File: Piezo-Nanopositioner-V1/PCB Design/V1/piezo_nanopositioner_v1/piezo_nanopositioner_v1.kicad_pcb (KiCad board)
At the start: 2 copper layers, 7 parts, among them J2 RF2-04A-T-00-50-G, U1 TDA2050, U2 DAC0800LCM, U3 TL431AIDBZR, U4 TL431AIDBZR

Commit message: finalized schematic, added hierarchical sheets for X,Y,Z circuit. Added all part fingerprints.
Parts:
- added C11: 47u, Capacitor_SMD:CAP_EEFC_E_PAN, F.Cu at (199.4, 137.6)
- added C13: 100uF 50V, Capacitor_THT:CAP_YX_8X11P5_RUB, F.Cu at (247.7, 123.4)
- added C14: 10n, Capacitor_SMD:C_0805_2012Metric, F.Cu at (186.8, 101.9)
- added C15: 100n, Capacitor_SMD:C_0805_2012Metric, F.Cu at (186.8, 104.9)
- added C16: 100n, Capacitor_SMD:C_0805_2012Metric, F.Cu at (186.8, 107.9)
- added C17: 470u, Capacitor_THT:CAP_ZSU_G12_PAN, F.Cu at (177.7, 106.5)
- added C18: 470u, Capacitor_THT:CAP_ZSU_G12_PAN, F.Cu at (177.7, 118.6)
- added C19: 68p, Capacitor_SMD:C_0805_2012Metric, F.Cu at (186.8, 110.9)
- added C20: 100n, Capacitor_SMD:C_0805_2012Metric, F.Cu at (186.8, 113.9)
- added C21: 100n, Capacitor_SMD:C_0805_2012Metric, F.Cu at (186.8, 116.9)
- added C22: 4.7n, Capacitor_SMD:C_0805_2012Metric, F.Cu at (186.8, 119.9)
- added C23: 47u, Capacitor_SMD:CAP_EEFC_E_PAN, F.Cu at (222.0, 89.0)
- added C24: 10n, Capacitor_SMD:C_0805_2012Metric, F.Cu at (209.4, 53.3)
- added C25: 100n, Capacitor_SMD:C_0805_2012Metric, F.Cu at (209.4, 56.3)
- added C26: 100n, Capacitor_SMD:C_0805_2012Metric, F.Cu at (209.4, 59.3)
- added C27: 470u, Capacitor_THT:CAP_ZSU_G12_PAN, F.Cu at (200.2, 57.8)
- added C28: 470u, Capacitor_THT:CAP_ZSU_G12_PAN, F.Cu at (200.2, 70.0)
- added C29: 68p, Capacitor_SMD:C_0805_2012Metric, F.Cu at (209.4, 62.3)
- added C30: 100n, Capacitor_SMD:C_0805_2012Metric, F.Cu at (209.4, 65.3)
- added C31: 100n, Capacitor_SMD:C_0805_2012Metric, F.Cu at (209.4, 68.3)
- added C32: 4.7n, Capacitor_SMD:C_0805_2012Metric, F.Cu at (209.4, 71.3)
- added C33: 47u, Capacitor_SMD:CAP_EEFC_E_PAN, F.Cu at (145.9, 90.5)
- added C34: 10n, Capacitor_SMD:C_0805_2012Metric, F.Cu at (133.2, 54.8)
- added C35: 100n, Capacitor_SMD:C_0805_2012Metric, F.Cu at (133.2, 57.8)
- added C36: 100n, Capacitor_SMD:C_0805_2012Metric, F.Cu at (133.2, 60.8)
- added C37: 470u, Capacitor_THT:CAP_ZSU_G12_PAN, F.Cu at (124.1, 59.0)
- added C38: 470u, Capacitor_THT:CAP_ZSU_G12_PAN, F.Cu at (110.5, 59.0)
- added C39: 68p, Capacitor_SMD:C_0805_2012Metric, F.Cu at (133.2, 63.8)
- added C40: 100n, Capacitor_SMD:C_0805_2012Metric, F.Cu at (133.2, 66.8)
- added C41: 100n, Capacitor_SMD:C_0805_2012Metric, F.Cu at (133.2, 69.8)
- added C42: 4.7n, Capacitor_SMD:C_0805_2012Metric, F.Cu at (133.2, 72.8)
- added D1: D, Diode_THT:DO-41_DIO, F.Cu at (246.1, 112.0)
- added D2: D, Diode_THT:DO-41_DIO, F.Cu at (246.1, 116.3)
- added J1: Conn_01x03_Pin, Connector_PinHeader_2.54mm:PinHeader_1x03_P2.54mm_Vertical, F.Cu at (256.8, 120.7)
- added J4: Conn_01x10_Pin, Connector_PinHeader_2.54mm:PinHeader_1x10_P2.54mm_Vertical, F.Cu at (167.8, 102.7)
- added J5: RF2-04A-T-00-50-G, RF:CONN_RF2-04A-T-00-50-G_ADM, F.Cu at (188.8, 137.3)
- added J6: Conn_01x10_Pin, Connector_PinHeader_2.54mm:PinHeader_1x10_P2.54mm_Vertical, F.Cu at (190.4, 54.1)
- added J7: RF2-04A-T-00-50-G, RF:CONN_RF2-04A-T-00-50-G_ADM, F.Cu at (211.4, 88.7)
- added J8: Conn_01x10_Pin, Connector_PinHeader_2.54mm:PinHeader_1x10_P2.54mm_Vertical, F.Cu at (117.4, 104.5)
- added J9: RF2-04A-T-00-50-G, RF:CONN_RF2-04A-T-00-50-G_ADM, F.Cu at (117.1, 48.6)
- added R14: 100R, Resistor_SMD:R_0805_2012Metric, F.Cu at (191.3, 101.8)
- added R15: 100R, Resistor_SMD:R_0805_2012Metric, F.Cu at (191.3, 104.8)
- added R16: 100R, Resistor_SMD:R_0805_2012Metric, F.Cu at (191.3, 107.8)
- added R17: 100R, Resistor_SMD:R_0805_2012Metric, F.Cu at (191.3, 110.7)
- added R18: 100R, Resistor_SMD:R_0805_2012Metric, F.Cu at (191.3, 113.7)
- added R19: 100R, Resistor_SMD:R_0805_2012Metric, F.Cu at (195.7, 101.8)
- added R20: 100R, Resistor_SMD:R_0805_2012Metric, F.Cu at (195.7, 104.8)
- added R21: 100R, Resistor_SMD:R_0805_2012Metric, F.Cu at (195.7, 107.8)
- added R22: 1k, Resistor_SMD:R_0805_2012Metric, F.Cu at (195.7, 110.7)
- added R23: 5k, Resistor_SMD:R_0805_2012Metric, F.Cu at (195.7, 113.7)
- added R24: 5k, Resistor_SMD:R_0805_2012Metric, F.Cu at (200.1, 101.8)
- added R25: 15k, Resistor_SMD:R_0805_2012Metric, F.Cu at (200.1, 104.8)
- added R26: 10R, Resistor_SMD:R_0805_2012Metric, F.Cu at (200.1, 107.8)
- added R27: 100R, Resistor_SMD:R_0805_2012Metric, F.Cu at (213.8, 53.2)
- added R28: 100R, Resistor_SMD:R_0805_2012Metric, F.Cu at (213.8, 56.2)
- added R29: 100R, Resistor_SMD:R_0805_2012Metric, F.Cu at (213.8, 59.1)
- added R30: 100R, Resistor_SMD:R_0805_2012Metric, F.Cu at (213.8, 62.1)
- added R31: 100R, Resistor_SMD:R_0805_2012Metric, F.Cu at (213.8, 65.0)
- added R32: 100R, Resistor_SMD:R_0805_2012Metric, F.Cu at (218.2, 53.2)
- added R33: 100R, Resistor_SMD:R_0805_2012Metric, F.Cu at (218.2, 56.2)
- added R34: 100R, Resistor_SMD:R_0805_2012Metric, F.Cu at (218.2, 59.1)
- added R35: 1k, Resistor_SMD:R_0805_2012Metric, F.Cu at (218.2, 62.1)
- added R36: 5k, Resistor_SMD:R_0805_2012Metric, F.Cu at (218.2, 65.0)
- added R37: 5k, Resistor_SMD:R_0805_2012Metric, F.Cu at (222.6, 53.2)
- added R38: 15k, Resistor_SMD:R_0805_2012Metric, F.Cu at (222.6, 56.2)
- added R39: 10R, Resistor_SMD:R_0805_2012Metric, F.Cu at (222.6, 59.1)
- added R40: 100R, Resistor_SMD:R_0805_2012Metric, F.Cu at (137.7, 54.7)
- added R41: 100R, Resistor_SMD:R_0805_2012Metric, F.Cu at (137.7, 57.7)
- added R42: 100R, Resistor_SMD:R_0805_2012Metric, F.Cu at (137.7, 60.6)
- added R43: 100R, Resistor_SMD:R_0805_2012Metric, F.Cu at (137.7, 63.6)
- added R44: 100R, Resistor_SMD:R_0805_2012Metric, F.Cu at (137.7, 66.5)
- added R45: 100R, Resistor_SMD:R_0805_2012Metric, F.Cu at (142.1, 54.7)
- added R46: 100R, Resistor_SMD:R_0805_2012Metric, F.Cu at (142.1, 57.7)
- added R47: 100R, Resistor_SMD:R_0805_2012Metric, F.Cu at (142.1, 60.6)
- added R48: 1k, Resistor_SMD:R_0805_2012Metric, F.Cu at (142.1, 63.6)
- added R49: 5k, Resistor_SMD:R_0805_2012Metric, F.Cu at (142.1, 66.5)
- added R50: 5k, Resistor_SMD:R_0805_2012Metric, F.Cu at (146.5, 54.7)
- added R51: 15k, Resistor_SMD:R_0805_2012Metric, F.Cu at (146.5, 57.7)
- added R52: 10R, Resistor_SMD:R_0805_2012Metric, F.Cu at (146.5, 60.6)
- added RV2: 10k, Potentiometer_THT:TRIM_COM-09806, F.Cu at (199.5, 127.0)
- added RV3: 10k, Potentiometer_THT:TRIM_COM-09806, F.Cu at (222.1, 78.4)
- added RV4: 10k, Potentiometer_THT:TRIM_COM-09806, F.Cu at (146.0, 79.9)
- added U10: TL431AIDBZR, TL431AIDBZR:DBZ0003A_N, F.Cu at (119.0, 90.5)
- added U11: DAC0800LCM, DAC0800LCM_SMT:M16A_TEX, F.Cu at (135.3, 80.2)
- added U12: TDA2050, Package_TO_SOT_THT:TO-220-5_P3.4x3.7mm_StaggerOdd_Lead3.8mm_Vertical, F.Cu at (118.9, 86.5)
- added U3: TL431AIDBZR, TL431AIDBZR:DBZ0003A_N, F.Cu at (172.6, 137.6)
- added U5: DAC0800LCM, DAC0800LCM_SMT:M16A_TEX, F.Cu at (188.9, 127.3)
- added U6: TDA2050, Package_TO_SOT_THT:TO-220-5_P3.4x3.7mm_StaggerOdd_Lead3.8mm_Vertical, F.Cu at (172.5, 133.7)
- added U7: TL431AIDBZR, TL431AIDBZR:DBZ0003A_N, F.Cu at (195.2, 89.0)
- added U8: DAC0800LCM, DAC0800LCM_SMT:M16A_TEX, F.Cu at (211.5, 78.7)
- added U9: TDA2050, Package_TO_SOT_THT:TO-220-5_P3.4x3.7mm_StaggerOdd_Lead3.8mm_Vertical, F.Cu at (195.1, 85.0)
- C12: value 50YXJ100MT78X11.5 -> 100uF 50V
- moved U4 83.9 mm to (56.5, 96.5)
- moved C12 83.9 mm to (43.0, 98.5)
- moved Heatsink 83.9 mm to (58.2, 74.5)
- moved J2 83.9 mm to (28.5, 98.0)
- moved U1 83.9 mm to (54.9, 86.2)
- moved U2 83.9 mm to (30.7, 71.1)
- moved U3 83.9 mm to (30.5, 81.0)
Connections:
- C12 pad 1: unconnected-(C12-Pad1) -> GND
- C12 pad 2: unconnected-(C12-Pad2) -> -15V

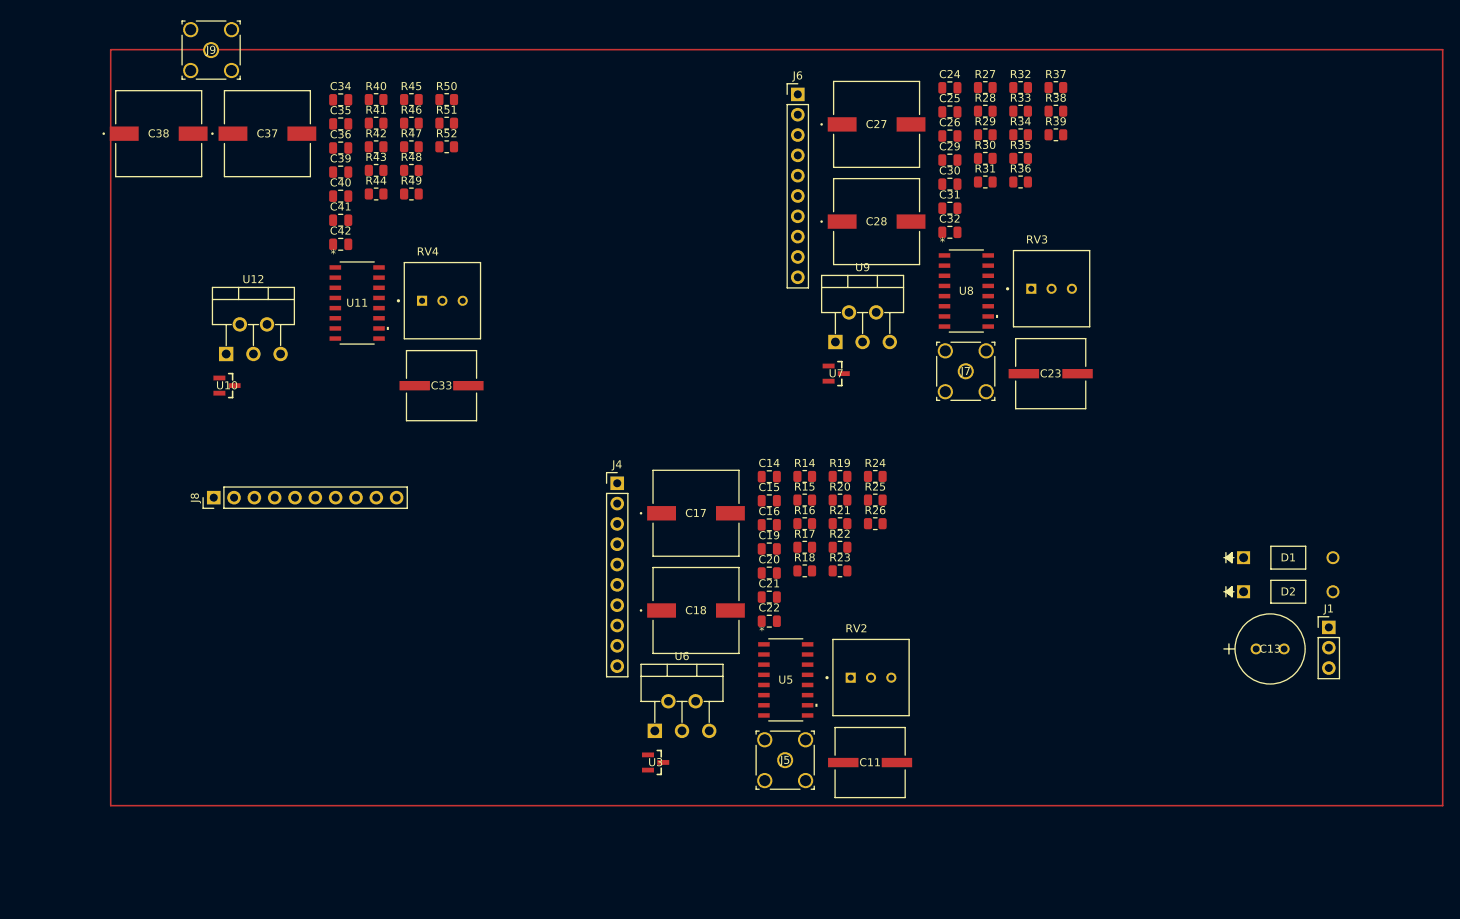
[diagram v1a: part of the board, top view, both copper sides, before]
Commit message: started PCB design, almost finished first DAC.
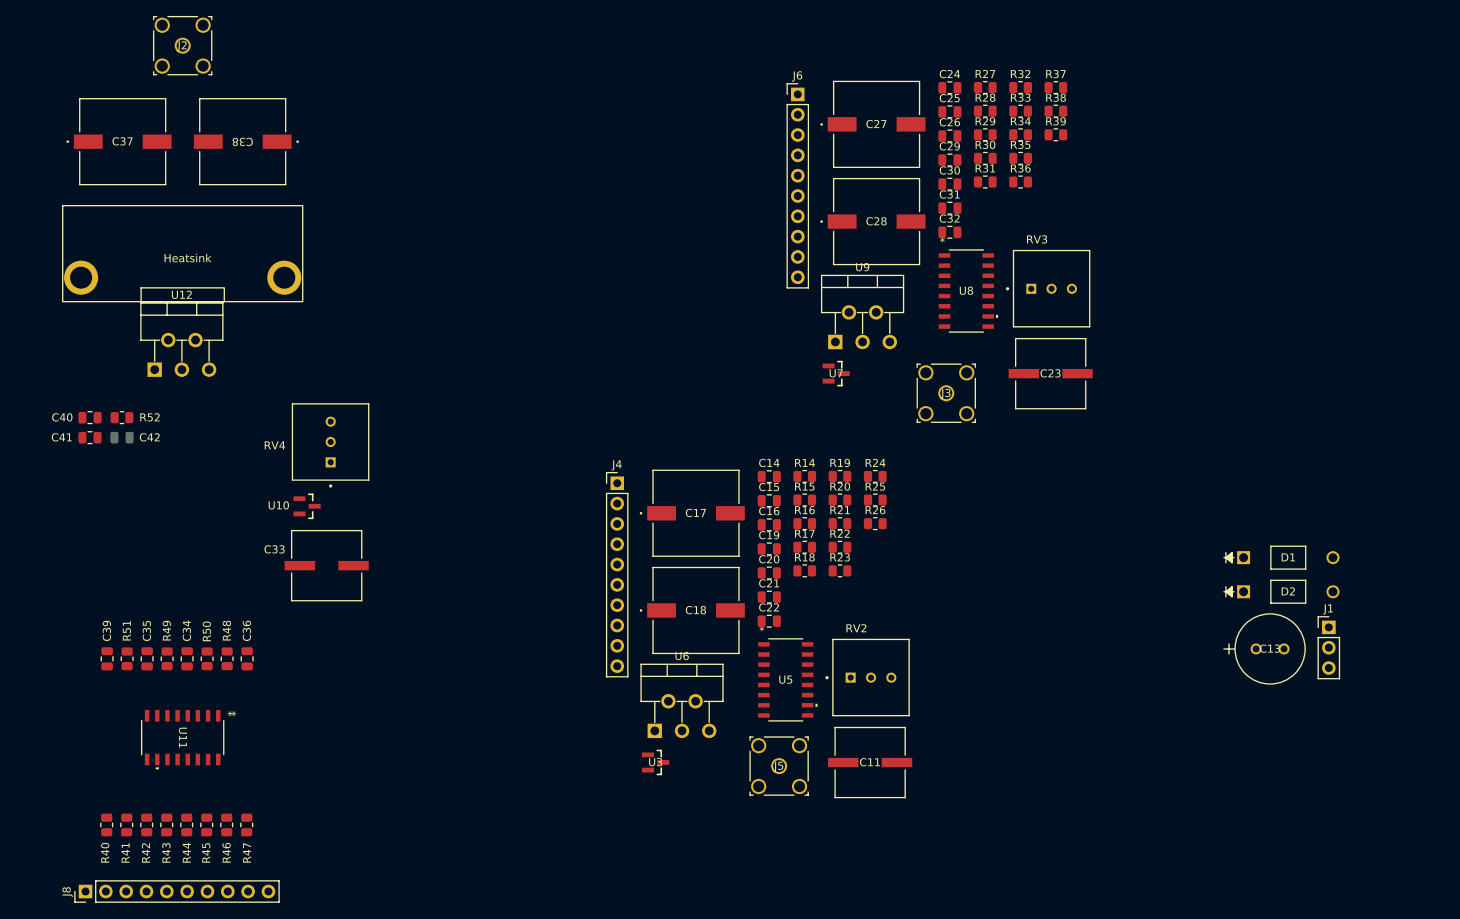
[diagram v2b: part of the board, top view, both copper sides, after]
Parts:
- removed J7, J9: RF2-04A-T-00-50-G, RF:CONN_RF2-04A-T-00-50-G_ADM
- added Heatsink: V6560Y, V6560Y:V6560Y, F.Cu at (113.5, 77.0)
- added J2: RF2-04A-T-00-50-G, RF:CONN_RF2-04A-T-00-50-G_ADM, F.Cu at (113.5, 48.0)
- added J3: RF2-04A-T-00-50-G, RF:CONN_RF2-04A-T-00-50-G_ADM, F.Cu at (208.9, 91.4)
- C42: moved to B.Cu
- moved R40 96.7 mm to (104.0, 145.4), turned to 90 degrees
- moved R45 94.2 mm to (116.5, 145.4), turned to 90 degrees
- moved R41 93.1 mm to (106.5, 145.4), turned to 90 degrees
- moved R46 90.7 mm to (119.0, 145.4), turned to 90 degrees
- moved R42 89.5 mm to (109.0, 145.4), turned to 90 degrees
- moved R47 87.2 mm to (121.5, 145.4), turned to 90 degrees
- moved R43 85.9 mm to (111.5, 145.4), turned to 90 degrees
- moved R44 82.4 mm to (114.0, 145.4), turned to 90 degrees
- moved R51 78.0 mm to (106.6, 124.6), turned to 90 degrees
- moved R50 76.0 mm to (116.6, 124.6), turned to 90 degrees
- moved C34 72.5 mm to (114.1, 124.6), turned to 90 degrees
- moved C35 71.1 mm to (109.1, 124.6), turned to -90 degrees
- moved C39 67.5 mm to (104.1, 124.6), turned to 90 degrees
- moved R49 65.6 mm to (111.6, 124.6), turned to -90 degrees
- moved R48 65.3 mm to (119.1, 124.6), turned to 90 degrees
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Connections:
- J5 pad 2: (no net) -> GND
- J5 pad 3: (no net) -> GND
- J5 pad 4: (no net) -> GND
- J5 pad 5: (no net) -> GND

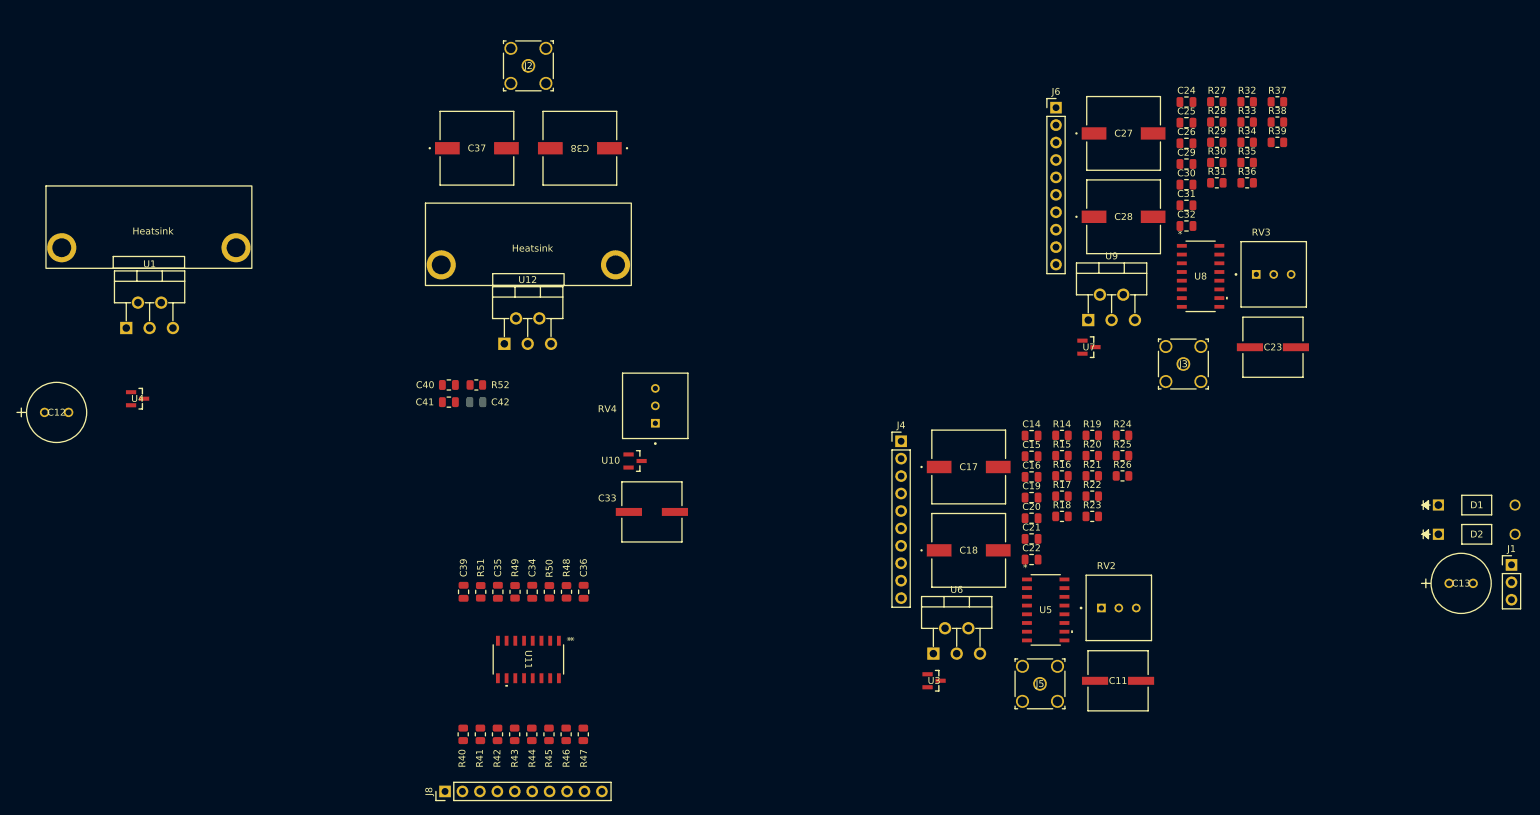
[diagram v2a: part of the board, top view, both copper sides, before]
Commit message: Created rough PCB component layout for Z actuator.
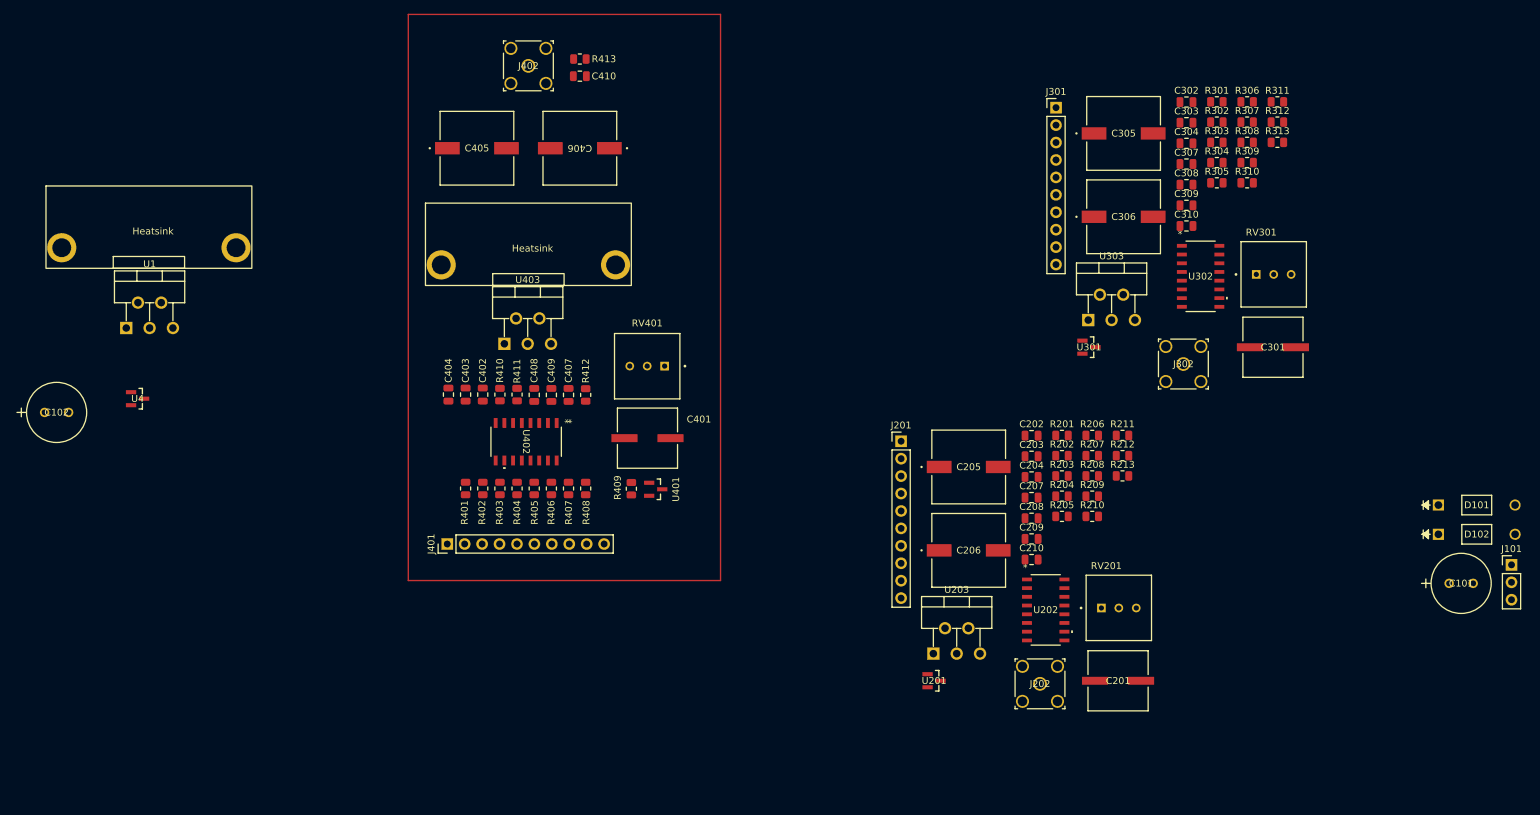
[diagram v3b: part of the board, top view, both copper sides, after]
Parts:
- C410: renamed from C42; moved to F.Cu
- moved C410 49.8 mm to (121.0, 49.5)
- moved R413 49.8 mm to (121.0, 47.0)
- moved J401 36.1 mm to (101.7, 117.7)
- moved R401 35.8 mm to (104.3, 109.6)
- moved R402 35.8 mm to (106.8, 109.6)
- moved R403 35.8 mm to (109.3, 109.6)
- moved R404 35.8 mm to (111.8, 109.6)
- moved R405 35.8 mm to (114.3, 109.6)
- moved R406 35.8 mm to (116.8, 109.6)
- moved R407 35.8 mm to (119.3, 109.6)
- moved R408 35.8 mm to (121.8, 109.6)
- moved C404 34.8 mm to (101.8, 95.9)
- moved C407 32.5 mm to (119.3, 96.0)
- moved R412 32.5 mm to (121.8, 96.0)
- moved U402 31.7 mm to (113.2, 102.8)
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- renumbered C13 to C101, C12 to C102, C11 to C201, C14 to C202, C15 to C203, C16 to C204, C17 to C205, C18 to C206, C19 to C207, C20 to C208, C21 to C209, C22 to C210, C23 to C301, C24 to C302, C25 to C303, C26 to C304, C27 to C305, C28 to C306, C29 to C307, C30 to C308, C31 to C309, C32 to C310, C33 to C401, C34 to C402, C35 to C403, C36 to C404, C37 to C405, C38 to C406, C39 to C407, C40 to C408, C41 to C409, D1 to D101, D2 to D102, J1 to J101, J4 to J201, J5 to J202, J6 to J301, J3 to J302, J8 to J401, J2 to J402, R14 to R201, R15 to R202, R16 to R203, R17 to R204, R18 to R205, R19 to R206, R20 to R207, R21 to R208, R22 to R209, R23 to R210, R24 to R211, R25 to R212, R26 to R213, R27 to R301, R28 to R302, R29 to R303, R30 to R304, R31 to R305, R32 to R306, R33 to R307, R34 to R308, R35 to R309, R36 to R310, R37 to R311, R38 to R312, R39 to R313, R40 to R401, R41 to R402, R42 to R403, R43 to R404, R44 to R405, R45 to R406, R46 to R407, R47 to R408, R48 to R409, R49 to R410, R50 to R411, R51 to R412, R52 to R413, RV2 to RV201, RV3 to RV301, RV4 to RV401, U3 to U201, U5 to U202, U6 to U203, U7 to U301, U8 to U302, U9 to U303, U10 to U401, U11 to U402, U12 to U403
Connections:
- J202 pad 2: GND -> (no net)
- J202 pad 3: GND -> (no net)
- J202 pad 4: GND -> (no net)
- J202 pad 5: GND -> (no net)
- J302 pad 2: GND -> (no net)
- J302 pad 3: GND -> (no net)
- J302 pad 4: GND -> (no net)
- J302 pad 5: GND -> (no net)
- J402 pad 2: GND -> (no net)
- J402 pad 3: GND -> (no net)
- J402 pad 4: GND -> (no net)
- J402 pad 5: GND -> (no net)
